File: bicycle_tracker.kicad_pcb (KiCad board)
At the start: 2 copper layers, 5 parts, among them U1 SAM-M8Q, U3 ICM-20948, U4 W25Q32JVZP, U5 ESP32-C6, U6 BQ24040

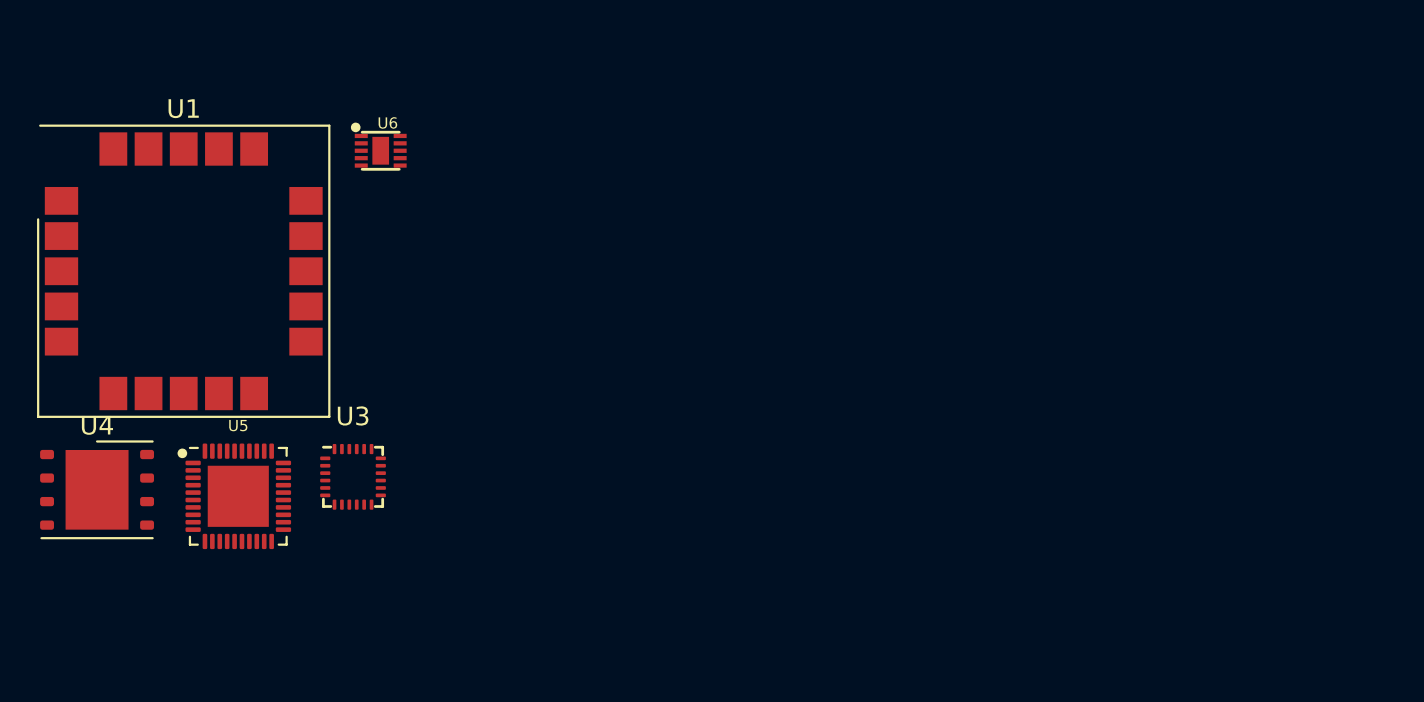
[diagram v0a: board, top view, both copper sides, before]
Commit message: Swapped to NRF and made a bunch of progress
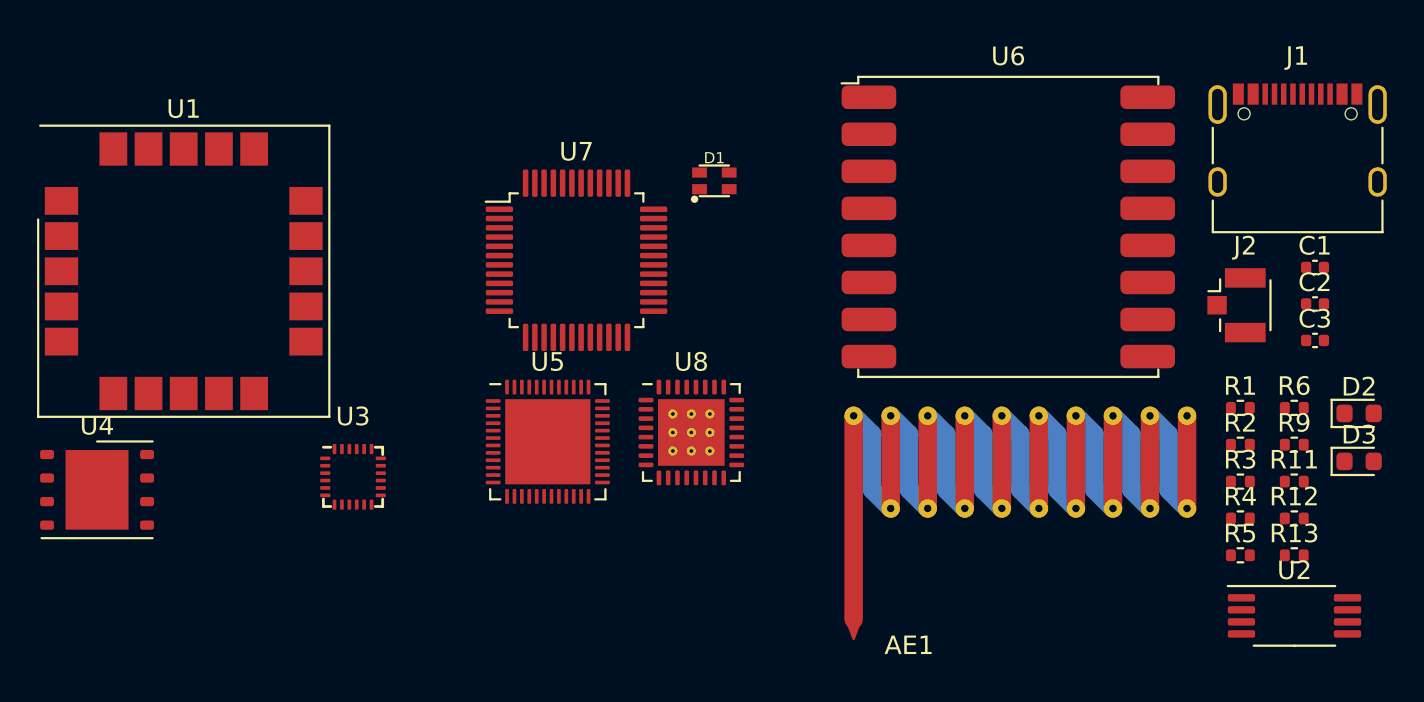
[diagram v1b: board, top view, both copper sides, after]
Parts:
- added AE1: ANT_SWRA416_RIGHT, RF_Antenna:Texas_SWRA416_868MHz_915MHz, F.Cu at (196.1, 111.8)
- added C1: 100nF, Capacitor_SMD:C_0402_1005Metric, F.Cu at (212.0, 98.0)
- added C2: DNP, Capacitor_SMD:C_0402_1005Metric, F.Cu at (212.0, 100.0)
- added C3: DNP, Capacitor_SMD:C_0402_1005Metric, F.Cu at (212.0, 102.0)
- added D1: LED_RGB_0606, bicycle_tracker:LED_0606, F.Cu at (179.6, 93.3)
- added D2: RX, LED_SMD:LED_0603_1608Metric, F.Cu at (214.4, 105.9)
- added D3: TX, LED_SMD:LED_0603_1608Metric, F.Cu at (214.4, 108.5)
- added J1: USB_C_KH-TYPE-C-16P, Connector_USB:USB_C_Receptacle_XKB_U262-16XN-4BVC11, F.Cu at (211.1, 92.3)
- added J2: ANT, Connector_Coaxial:U.FL_Hirose_U.FL-R-SMT-1_Vertical, F.Cu at (207.8, 100.1)
- added R1: 100R, Resistor_SMD:R_0402_1005Metric, F.Cu at (208.0, 105.6)
- added R11: 470R, Resistor_SMD:R_0402_1005Metric, F.Cu at (210.9, 109.6)
- added R12: 1k, Resistor_SMD:R_0402_1005Metric, F.Cu at (210.9, 111.6)
- added R13: 1k, Resistor_SMD:R_0402_1005Metric, F.Cu at (210.9, 113.6)
- added R2: 100R, Resistor_SMD:R_0402_1005Metric, F.Cu at (208.0, 107.6)
- added R3: 100R, Resistor_SMD:R_0402_1005Metric, F.Cu at (208.0, 109.6)
- added R4: 5k1, Resistor_SMD:R_0402_1005Metric, F.Cu at (208.0, 111.6)
- added R5: 5k1, Resistor_SMD:R_0402_1005Metric, F.Cu at (208.0, 113.6)
- added R6: 1k, Resistor_SMD:R_0402_1005Metric, F.Cu at (210.9, 105.6)
- added R9: 0R, Resistor_SMD:R_0402_1005Metric, F.Cu at (210.9, 107.6)
- added U2: 24LC64, Package_SO:TSSOP-8_4.4x3mm_P0.65mm, F.Cu at (210.9, 116.8)
- added U7: FT2232D, Package_QFP:LQFP-48_7x7mm_P0.5mm, F.Cu at (172.2, 97.6)
- added U8: nPM1300-QEXX, Package_DFN_QFN:QFN-32-1EP_5x5mm_P0.5mm_EP3.6x3.6mm_ThermalVias, F.Cu at (178.4, 106.9)
- U1: value SAM-M8Q -> SAM-M10Q
- U5: value ESP32-C6 -> nRF52832-QFXX; footprint bicycle_tracker:QFN-40-1EP_5x5mm_P0.4mm_EP3.3x3.3mm -> Package_DFN_QFN:QFN-48-1EP_6x6mm_P0.4mm_EP4.6x4.6mm
- U6: value BQ24040 -> RFM95W-868S2; footprint bicycle_tracker:PWSON-N10-2x2 -> RF_Module:HOPERF_RFM9XW_SMD
- moved U6 34.1 mm to (195.5, 95.8)
- moved U5 17.0 mm to (170.6, 107.4)
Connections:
- U1 pad 1: Net-(U1-GND-Pad1) -> GND
- U1 pad 10: Net-(U1-GND-Pad1) -> GND
- U1 pad 11: Net-(U1-GND-Pad1) -> GND
- U1 pad 12: unconnected-(U1-SCL-Pad12) -> /I2C_SCL
- U1 pad 15: Net-(U1-GND-Pad1) -> GND
- U1 pad 16: Net-(U1-GND-Pad1) -> GND
- U1 pad 17: unconnected-(U1-VCC-Pad17) -> +3V3
- U1 pad 18: unconnected-(U1-~{RESET}-Pad18) -> /~{GPS_RESET}
- U1 pad 19: unconnected-(U1-EXTINT-Pad19) -> /~{GPS_INT}
- U1 pad 2: unconnected-(U1-VCC_IO-Pad2) -> +3V3
- U1 pad 20: Net-(U1-GND-Pad1) -> GND
- U1 pad 4: Net-(U1-GND-Pad1) -> GND
- U1 pad 5: Net-(U1-GND-Pad1) -> GND
- U1 pad 6: Net-(U1-GND-Pad1) -> GND
- U1 pad 7: unconnected-(U1-TIMEPULSE-Pad7) -> /GPS_TIMEPULSE
- U1 pad 8: unconnected-(U1-~{SAFEBOOT}-Pad8) -> /~{GPS_SAFEBOOT}
- U1 pad 9: unconnected-(U1-SDA-Pad9) -> /I2C_SDA
- U3 pad 11: unconnected-(U3-FSYNC-Pad11) -> GND
- U3 pad 12: unconnected-(U3-INT1-Pad12) -> /IMU_INT
- U3 pad 13: unconnected-(U3-VDD-Pad13) -> +3V3
- U3 pad 18: Net-(U3-GND-Pad18) -> GND
- U3 pad 20: Net-(U3-GND-Pad18) -> GND
- U3 pad 22: unconnected-(U3-~{CS}-Pad22) -> +1V8
- U3 pad 23: unconnected-(U3-SCL/SCLK-Pad23) -> /I2C_SCL
- U3 pad 24: unconnected-(U3-SDA/SDI-Pad24) -> /I2C_SDA
- U3 pad 8: unconnected-(U3-VDDIO-Pad8) -> +1V8
- U3 pad 9: unconnected-(U3-SDO/AD0-Pad9) -> +1V8
- U4 pad 1: Net-(U4-~{CS}) -> /~{QSPI_CS}
- U4 pad 2: Net-(U4-DO(IO1)) -> /QSPI_IO1
- U4 pad 3: Net-(U4-IO2) -> /QSPI_IO2
- U4 pad 4: unconnected-(U4-GND-Pad4) -> GND
- U4 pad 5: Net-(U4-DI(IO0)) -> /QSPI_IO0
- U4 pad 6: Net-(U4-CLK) -> /QSPI_SCLK
- U4 pad 7: Net-(U4-IO3) -> /QSPI_IO3
- U4 pad 8: Net-(U4-VCC) -> /VDD_SPI
- U4 pad 9: unconnected-(U4-EP-Pad9) -> GND
- U5 pad 10: /UART_MRXSTX -> unconnected-(U5-P0.08-Pad10)
- U5 pad 11: /UART_MTXSRX -> unconnected-(U5-NFC1/P0.09-Pad11)
- U5 pad 12: /I2C_SDA -> unconnected-(U5-NFC2/P0.10-Pad12)
- U5 pad 13: /I2C_SCL -> Net-(U5-VDD-Pad13)
- U5 pad 20: Net-(U4-~{CS}) -> unconnected-(U5-P0.17-Pad20)
- U5 pad 21: Net-(U4-DO(IO1)) -> unconnected-(U5-P0.18/TRACEDATA[0]-Pad21)
- U5 pad 22: Net-(U4-IO2) -> unconnected-(U5-P0.19-Pad22)
- U5 pad 23: Net-(U4-VCC) -> unconnected-(U5-P0.20/TRACECLK-Pad23)
- U5 pad 24: Net-(U4-IO3) -> Net-(U5-P0.21/~{RESET})
- U5 pad 25: Net-(U4-CLK) -> unconnected-(U5-SWDCLK-Pad25)
- U5 pad 26: Net-(U4-DI(IO0)) -> unconnected-(U5-SWDIO-Pad26)
- U5 pad 31: unconnected-(U5-GPIO18-Pad31) -> Net-(U5-VSS-Pad31)
- U5 pad 36: unconnected-(U5-GPIO23-Pad36) -> Net-(U5-VDD-Pad13)
- U6 pad 1: unconnected-(U6-VIN-Pad1) -> GND
- U6 pad 10: unconnected-(U6-VOUT-Pad10) -> GND
- U6 pad 2: unconnected-(U6-ISET-Pad2) -> /LORA_SPI_MISO
- U6 pad 3: unconnected-(U6-VSS-Pad3) -> /LORA_SPI_MOSI
- U6 pad 4: unconnected-(U6-PRE-TERM-Pad4) -> /LORA_SPI_SCK
- U6 pad 5: unconnected-(U6-~{PG}-Pad5) -> /~{LORA_SPI_CS}
- U6 pad 6: unconnected-(U6-NC-Pad6) -> /~{LORA_RESET}
- U6 pad 8: unconnected-(U6-~{CHG}-Pad8) -> GND
- U6 pad 9: unconnected-(U6-TS-Pad9) -> Net-(U6-ANT)
